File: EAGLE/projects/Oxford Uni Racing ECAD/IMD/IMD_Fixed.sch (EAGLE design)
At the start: 37 parts, among them IC1 LM2901N, IC2 555, J2 T821108A1S100CEU, K1 RT444012, T1 IRLML6402, X1 Connector i, X2 GREEN_LIGHTS, X3 RED_LIGHTS

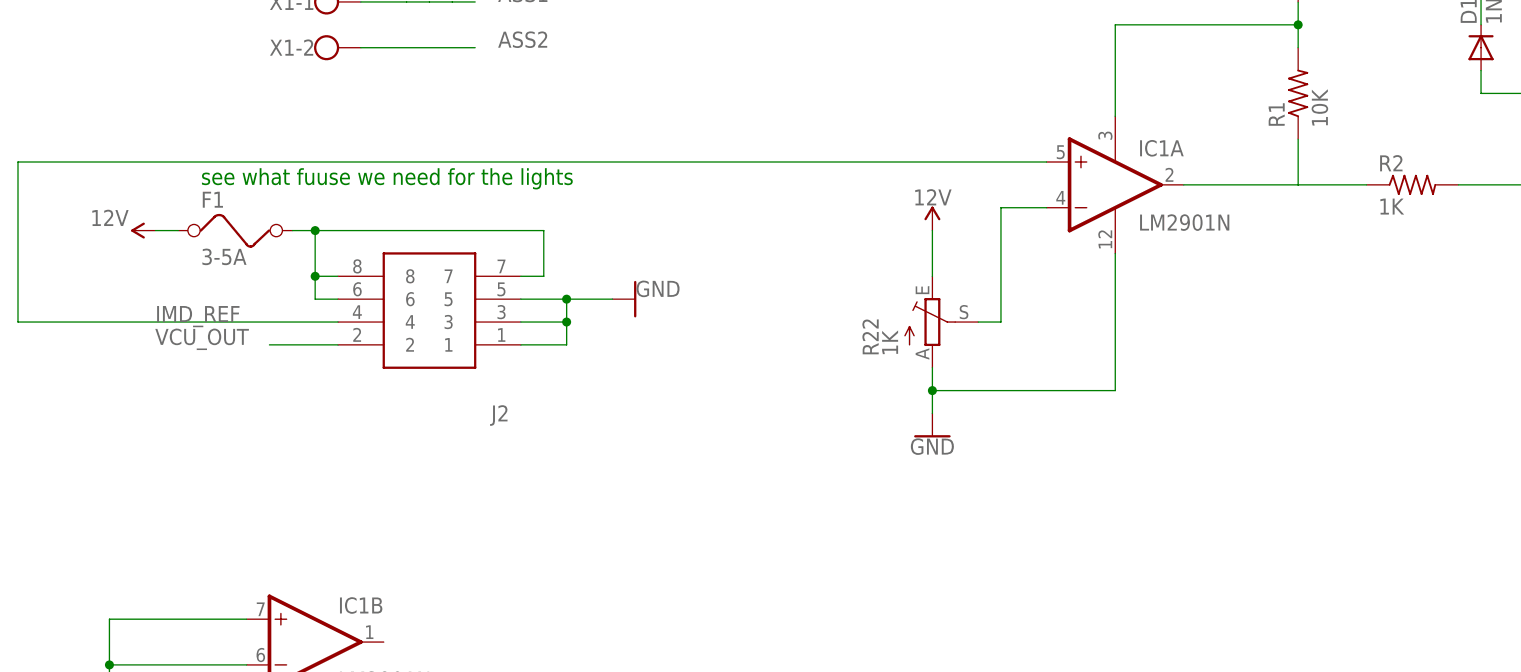
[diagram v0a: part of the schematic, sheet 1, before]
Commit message: routed IMD
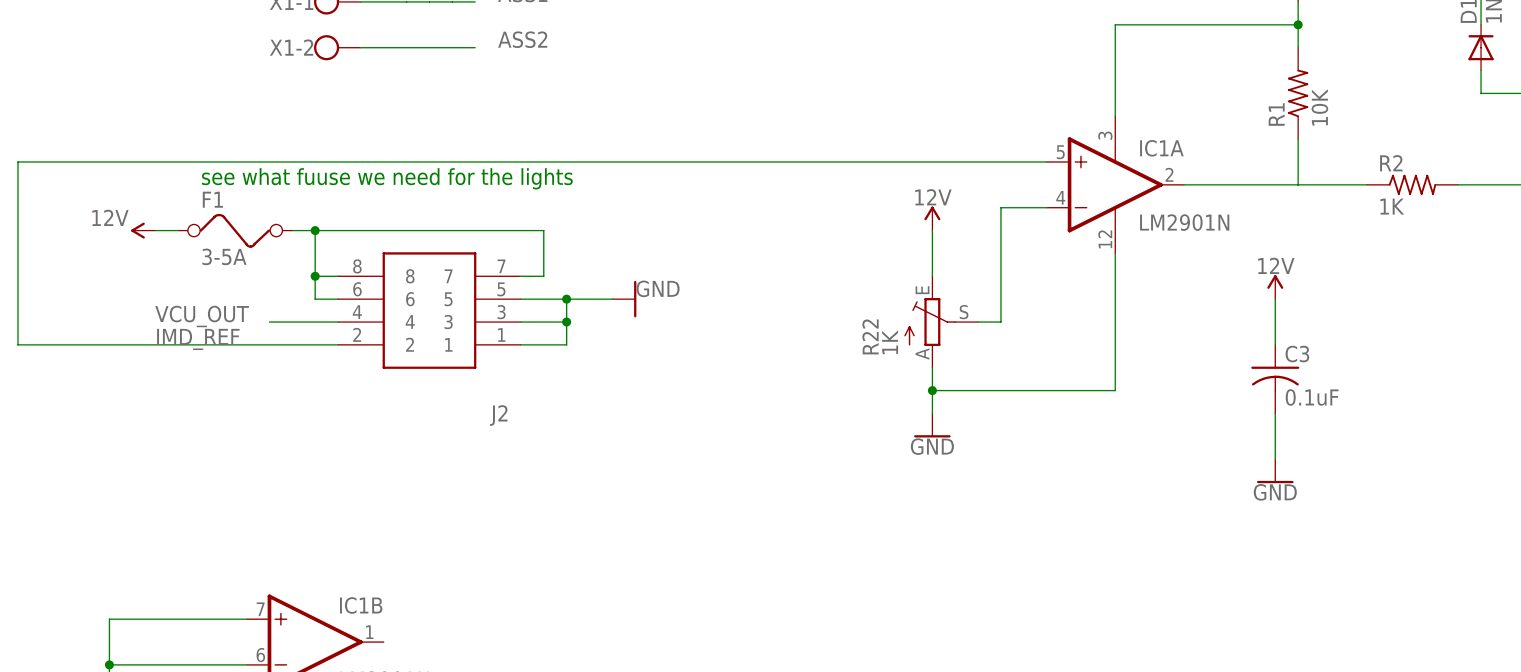
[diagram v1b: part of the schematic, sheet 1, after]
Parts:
- added C3: 0.1uF, adafruit:C-US050-024X044
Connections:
- net 12V: now also C3.1
- net GND: now also C3.2
- net IMD_REF: now also J2.2; no longer J2.4
- net VCU_OUT: now also J2.4; no longer J2.2
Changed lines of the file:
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@@
 <part name="SUPPLY5" library="SparkFun-PowerSymbols" library_urn="urn:adsk.eagle:library:530" deviceset="12V" device=""/>
 <part name="SUPPLY6" library="SparkFun-PowerSymbols" library_urn="urn:adsk.eagle:library:530" deviceset="12V" device=""/>
-<part name="SUPPLY7" library="SparkFun-PowerSymbols" library_urn="urn:adsk.eagle:library:530" deviceset="12V" device=""/>
 <part name="SUPPLY8" library="SparkFun-PowerSymbols" library_urn="urn:adsk.eagle:library:530" deviceset="12V" device=""/>
 <part name="GND4" library="SparkFun-PowerSymbols" library_urn="urn:adsk.eagle:library:530" deviceset="GND" device=""/>
@@
 <part name="X2" library="con-wago-500" library_urn="urn:adsk.eagle:library:195" deviceset="W237-102" device="" package3d_urn="urn:adsk.eagle:package:10688/1" value="GREEN_LIGHTS"/>
 <part name="X3" library="con-wago-500" library_urn="urn:adsk.eagle:library:195" deviceset="W237-102" device="" package3d_urn="urn:adsk.eagle:package:10688/1" value="RED_LIGHTS"/>
+<part name="C3" library="adafruit" library_urn="urn:adsk.eagle:library:420" deviceset="C-US" device="050-024X044" package3d_urn="urn:adsk.eagle:package:6240356/1" value="0.1uF"/>
+<part name="SUPPLY10" library="SparkFun-PowerSymbols" library_urn="urn:adsk.eagle:library:530" deviceset="12V" device=""/>
+<part name="GND9" library="SparkFun-PowerSymbols" library_urn="urn:adsk.eagle:library:530" deviceset="GND" device=""/>
 </parts>
 <sheets>
@@
 <instance part="GND3" gate="1" x="17.78" y="33.02" smashed="yes">
 <attribute name="VALUE" x="17.78" y="32.766" size="1.778" layer="96" align="top-center"/>
+</instance>
+<instance part="C3" gate="G$1" x="147.32" y="111.76" smashed="yes">
+<attribute name="NAME" x="148.336" y="112.395" size="1.778" layer="95"/>
+<attribute name="VALUE" x="148.336" y="107.569" size="1.778" layer="96"/>
+</instance>
+<instance part="SUPPLY10" gate="G$1" x="147.32" y="119.38" smashed="yes">
+<attribute name="VALUE" x="147.32" y="122.174" size="1.778" layer="96" align="bottom-center"/>
+</instance>
+<instance part="GND9" gate="1" x="147.32" y="99.06" smashed="yes">
+<attribute name="VALUE" x="147.32" y="98.806" size="1.778" layer="96" align="top-center"/>
 </instance>
 </instances>
@@
 <junction x="17.78" y="43.18"/>
 </segment>
+<segment>
+<pinref part="GND9" gate="1" pin="GND"/>
+<pinref part="C3" gate="G$1" pin="2"/>
+<wire x1="147.32" y1="101.6" x2="147.32" y2="106.68" width="0.1524" layer="91"/>
+</segment>
 </net>
 <net name="N$1" class="0">
@@
 <wire x1="25.4" y1="127" x2="22.86" y2="127" width="0.1524" layer="91"/>
 </segment>
+<segment>
+<pinref part="C3" gate="G$1" pin="1"/>
+<pinref part="SUPPLY10" gate="G$1" pin="12V"/>
+<wire x1="147.32" y1="114.3" x2="147.32" y2="119.38" width="0.1524" layer="91"/>
+</segment>
 </net>
 <net name="ASS1" class="0">
@@
 <segment>
 <pinref part="IC1" gate="A" pin="+IN"/>
-<label x="22.86" y="116.84" size="1.778" layer="95"/>
-<wire x1="7.62" y1="116.84" x2="7.62" y2="134.62" width="0.1524" layer="91"/>
+<label x="22.86" y="114.3" size="1.778" layer="95"/>
+<wire x1="7.62" y1="114.3" x2="7.62" y2="134.62" width="0.1524" layer="91"/>
 <wire x1="7.62" y1="134.62" x2="121.92" y2="134.62" width="0.1524" layer="91"/>
-<pinref part="J2" gate="G$1" pin="4"/>
-<wire x1="43.18" y1="116.84" x2="7.62" y2="116.84" width="0.1524" layer="91"/>
+<pinref part="J2" gate="G$1" pin="2"/>
+<wire x1="43.18" y1="114.3" x2="7.62" y2="114.3" width="0.1524" layer="91"/>
 </segment>
 </net>
@@
 <net name="VCU_OUT" class="0">
 <segment>
-<pinref part="J2" gate="G$1" pin="2"/>
-<wire x1="43.18" y1="114.3" x2="35.56" y2="114.3" width="0.1524" layer="91"/>
-<label x="22.86" y="114.3" size="1.778" layer="95"/>
+<wire x1="43.18" y1="116.84" x2="35.56" y2="116.84" width="0.1524" layer="91"/>
+<label x="22.86" y="116.84" size="1.778" layer="95"/>
+<pinref part="J2" gate="G$1" pin="4"/>
 </segment>
 </net>
@@
 <attribute name="VALUE" x="236.22" y="-75.946" size="1.778" layer="96" align="bottom-center"/>
 </instance>
-<instance part="SUPPLY7" gate="G$1" x="160.02" y="5.08" smashed="yes">
-<attribute name="VALUE" x="160.02" y="7.874" size="1.778" layer="96" align="bottom-center"/>
-</instance>
 <instance part="SUPPLY8" gate="G$1" x="200.66" y="45.72" smashed="yes">
